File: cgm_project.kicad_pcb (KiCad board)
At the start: 2 copper layers, 50 x 70 mm, 34 parts, among them J1 JST BATT CONNECTOR, J2 USB_C_Receptacle_USB2.0_16P, J3 Conn_01x02, J4 Conn_01x02_MountingPin, Q1 AO3400, SW1 SW_SPDT, SW2 BOOT, SW3 RESET, U1 TP4056-42-ESOP8, U2 AP2112K-3.3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

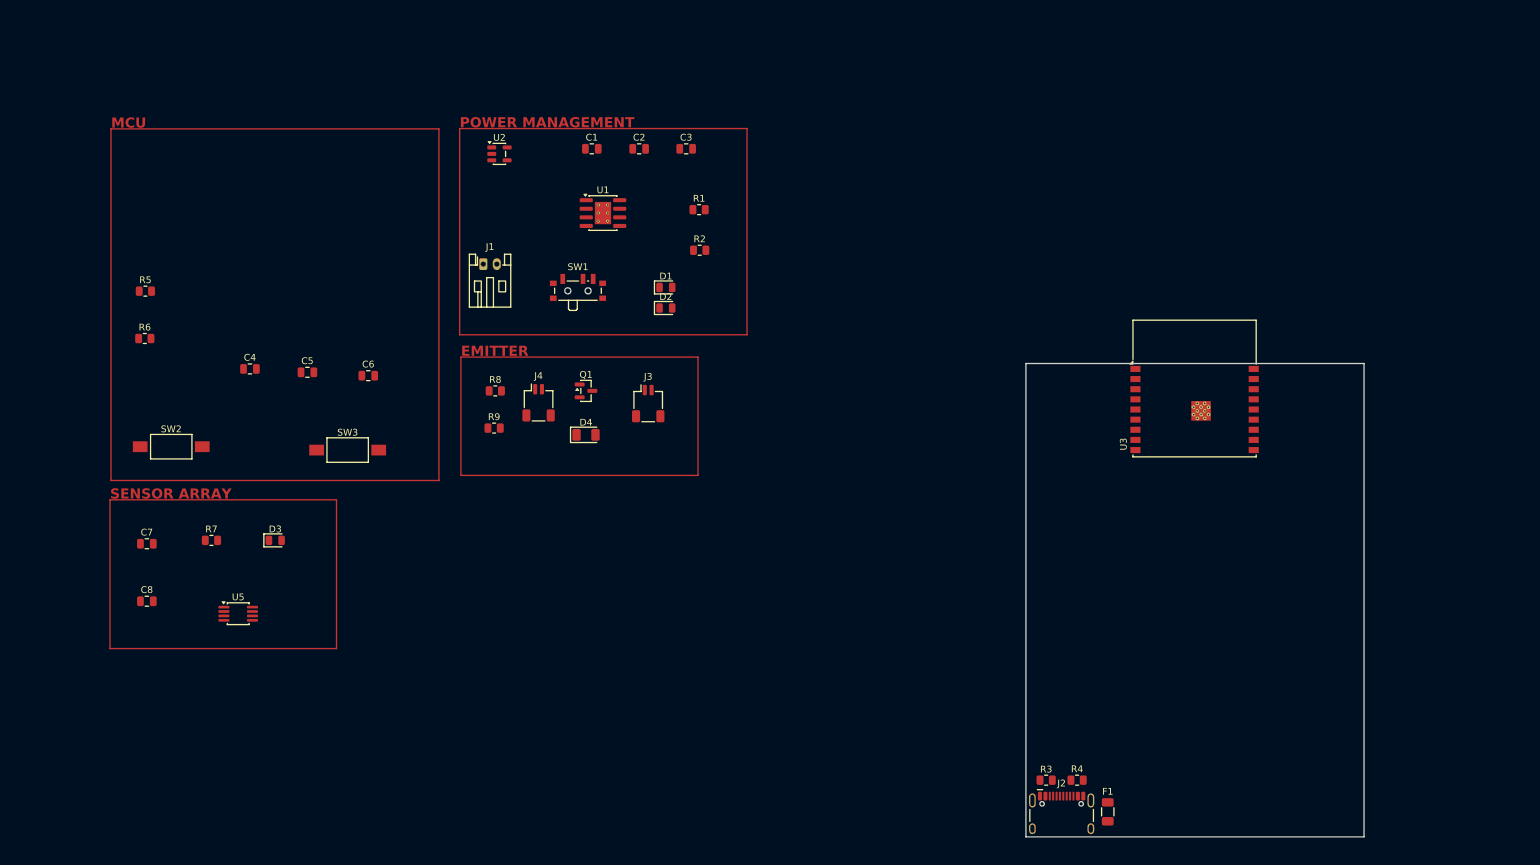
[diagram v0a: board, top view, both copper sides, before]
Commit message: chore: finalize component placement for power management, USB interface
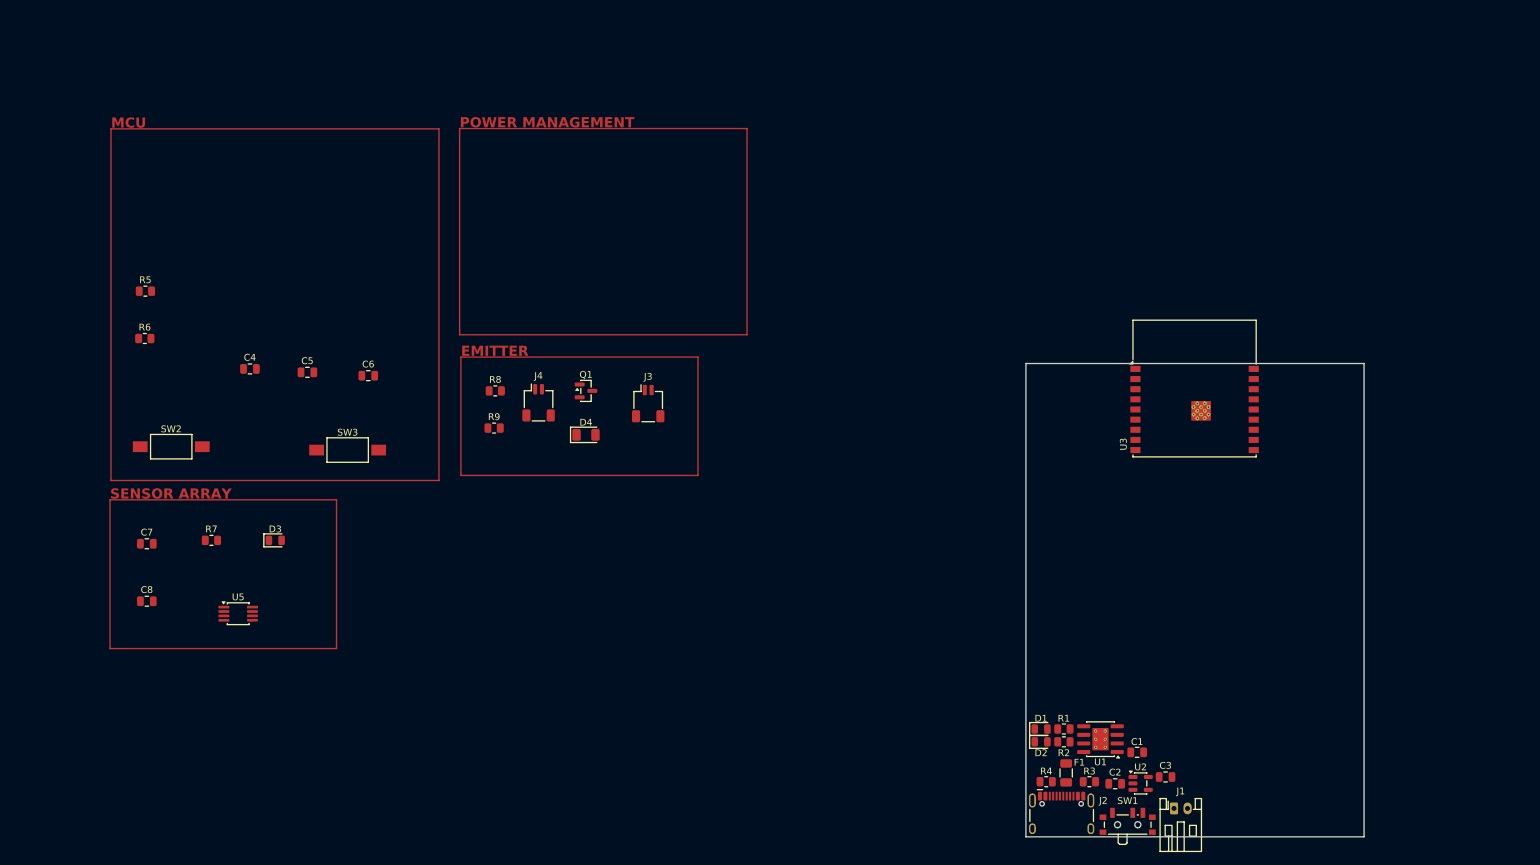
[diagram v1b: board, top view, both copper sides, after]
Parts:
- moved U2 132.9 mm to (167.0, 112.1)
- moved J1 130.1 mm to (171.9, 115.8)
- moved C1 120.3 mm to (166.4, 107.5), turned to 180 degrees
- moved C2 117.4 mm to (163.2, 112.2)
- moved C3 116.9 mm to (170.7, 111.2)
- moved SW1 113.3 mm to (165.1, 117.9)
- moved U1 107.1 mm to (161.0, 105.6), turned to 180 degrees
- moved R1 93.9 mm to (155.6, 104.0)
- moved R2 90.5 mm to (155.6, 106.0)
- moved D1 85.7 mm to (152.2, 104.1)
- moved D2 84.8 mm to (152.2, 106.0)
- moved F1 8.42 mm to (155.9, 110.5), turned to -90 degrees
- moved R3 6.40 mm to (159.4, 111.8)
- moved R4 4.57 mm to (153.0, 111.8), turned to 180 degrees

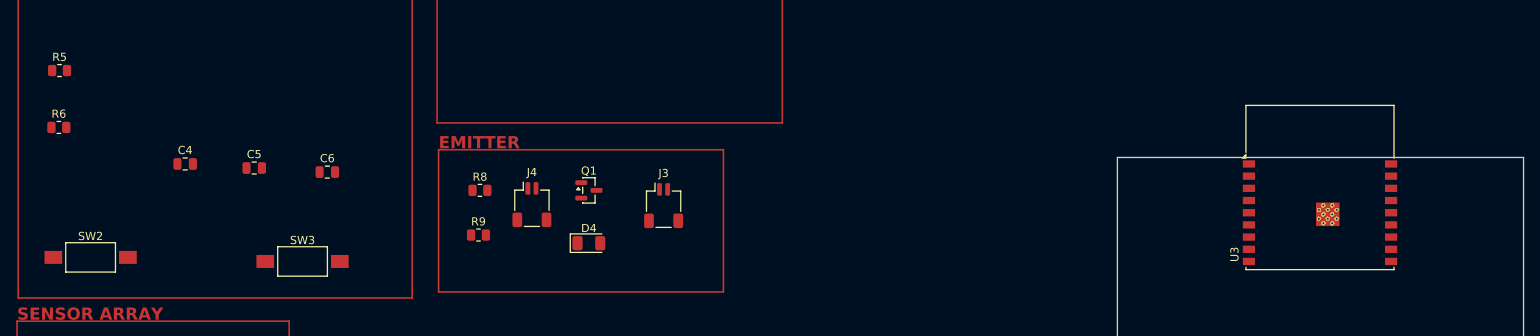
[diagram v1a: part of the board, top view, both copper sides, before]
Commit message: chore: finalize ESP32-C3 MCU layout, boot logic, and decoupling
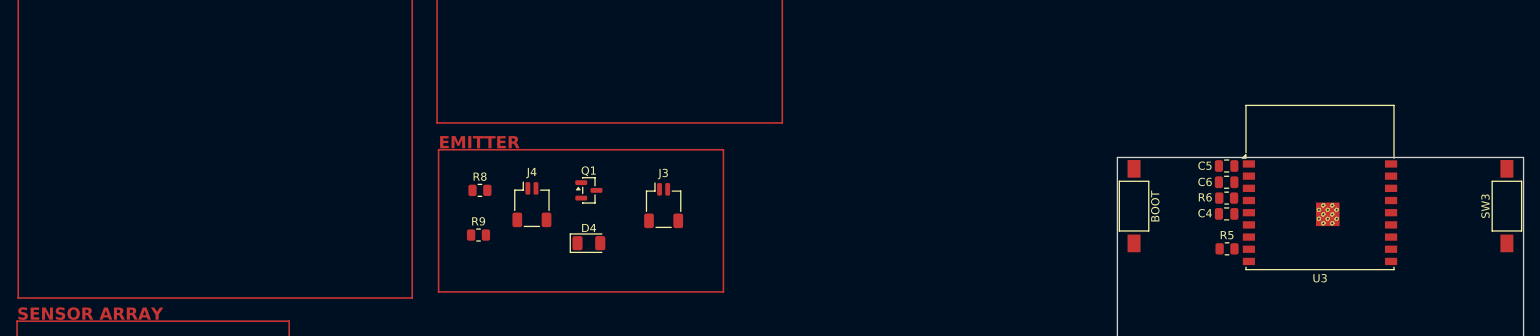
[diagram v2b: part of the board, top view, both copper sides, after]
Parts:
- moved SW3 148.4 mm to (197.9, 56.0), turned to 90 degrees
- moved R5 145.4 mm to (163.5, 61.2)
- moved R6 144.0 mm to (163.4, 55.0), turned to 180 degrees
- moved BOOT 128.6 mm to (152.1, 56.0), turned to 90 degrees
- moved C4 128.4 mm to (163.4, 57.0), turned to 180 degrees
- moved C5 119.7 mm to (163.4, 51.0), turned to 180 degrees
- moved C6 110.7 mm to (163.4, 53.0)
- renumbered SW2 to BOOT

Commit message: chore: finalize placement for analog sensor array
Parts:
- moved C7 161.9 mm to (177.3, 114.8), turned to -90 degrees
- moved C8 160.7 mm to (178.4, 112.1), turned to 180 degrees
- moved R7 157.3 mm to (182.7, 112.1)
- moved U5 150.6 mm to (181.5, 114.8), turned to 180 degrees
- moved D3 149.6 mm to (182.7, 117.5)
- moved C2 0.36 mm to (163.0, 111.8)
- renumbered SW3 to RESET
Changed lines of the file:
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@@
 	(footprint "Capacitor_SMD:C_0805_2012Metric"
 		(layer "F.Cu")
-		(at 19.995 76.655)
+		(at 177.35 114.8 -90)
 		(descr "Capacitor SMD 0805 (2012 Metric), square (rectangular) end terminal, IPC-7351 nominal, (Body size source: IPC-SM-782 page 76, https://www.pcb-3d.com/wordpress/wp-content/uploads/ipc-sm-782a_amendment_1_and_2.pdf, https://docs.google.com/spreadsheets/d/1BsfQQcO9C6DZCsRaXUlFlo91Tg2WpOkGARC1WS5S8t0/edit?usp=sharing)")
 		(tags "capacitor")
 		(property "Reference" "C7"
-			(at 0 -1.68 0)
+			(at 2.4 -0.05 180)
 			(layer "F.SilkS")
 			(effects
@@
 		)
 		(property "Value" "0.1uF"
-			(at -0.5 12.63 0)
+			(at -0.5 12.63 90)
 			(layer "F.Fab")
 			(effects
@@
 		)
 		(property "Datasheet" ""
-			(at 0 0 0)
+			(at 0 0 90)
 			(layer "F.Fab")
 			(hide yes)
@@
 		)
 		(property "Description" "Unpolarized capacitor, small symbol"
-			(at 0 0 0)
+			(at 0 0 90)
 			(layer "F.Fab")
 			(hide yes)
@@
 		)
 		(property "KiLib_Generator" "SMD_2terminal_chip_molded"
-			(at 0 0 0)
+			(at 0 0 90)
 			(layer "F.SilkS")
 			(hide yes)
@@
 		(duplicate_pad_numbers_are_jumpers no)
 		(fp_line
-			(start -0.261252 -0.735)
-			(end 0.261252 -0.735)
+			(start -0.261252 0.735)
+			(end 0.261252 0.735)
 			(stroke
 				(width 0.12)
@@
 		)
 		(fp_line
-			(start -0.261252 0.735)
-			(end 0.261252 0.735)
+			(start -0.261252 -0.735)
+			(end 0.261252 -0.735)
 			(stroke
 				(width 0.12)
@@
 		)
 		(fp_text user "${REFERENCE}"
-			(at 0 0 0)
+			(at 0 0 90)
 			(layer "F.Fab")
 			(effects
@@
 		)
 		(pad "1" smd roundrect
-			(at -0.95 0)
+			(at -0.95 0 270)
 			(size 1 1.45)
 			(layers "F.Cu" "F.Mask" "F.Paste")
@@
 		)
 		(pad "2" smd roundrect
-			(at 0.95 0)
+			(at 0.95 0 270)
 			(size 1 1.45)
 			(layers "F.Cu" "F.Mask" "F.Paste")
@@
 	(footprint "Capacitor_SMD:C_0805_2012Metric"
 		(layer "F.Cu")
-		(at 19.995 85.155)
+		(at 178.4 112.1 180)
 		(descr "Capacitor SMD 0805 (2012 Metric), square (rectangular) end terminal, IPC-7351 nominal, (Body size source: IPC-SM-782 page 76, https://www.pcb-3d.com/wordpress/wp-content/uploads/ipc-sm-782a_amendment_1_and_2.pdf, https://docs.google.com/spreadsheets/d/1BsfQQcO9C6DZCsRaXUlFlo91Tg2WpOkGARC1WS5S8t0/edit?usp=sharing)")
 		(tags "capacitor")
 		(property "Reference" "C8"
-			(at 0 -1.68 0)
+			(at 0 1.6 180)
 			(layer "F.SilkS")
 			(effects
@@
 		(duplicate_pad_numbers_are_jumpers no)
 		(fp_line
-			(start -0.261252 -0.735)
-			(end 0.261252 -0.735)
+			(start -0.261252 0.735)
+			(end 0.261252 0.735)
 			(stroke
 				(width 0.12)
@@
 		)
 		(fp_line
-			(start -0.261252 0.735)
-			(end 0.261252 0.735)
+			(start -0.261252 -0.735)
+			(end 0.261252 -0.735)
 			(stroke
 				(width 0.12)
@@
 		)
 		(pad "1" smd roundrect
-			(at -0.95 0)
+			(at -0.95 0 180)
 			(size 1 1.45)
 			(layers "F.Cu" "F.Mask" "F.Paste")
@@
 		)
 		(pad "2" smd roundrect
-			(at 0.95 0)
+			(at 0.95 0 180)
 			(size 1 1.45)
 			(layers "F.Cu" "F.Mask" "F.Paste")
@@
 	(footprint "Package_SO:MSOP-8_3x3mm_P0.65mm"
 		(layer "F.Cu")
-		(at 33.5 87)
+		(at 181.5125 114.825 180)
 		(descr "MSOP, 8 Pin (https://www.jedec.org/system/files/docs/mo-187F.pdf variant AA)")
 		(tags "MSOP SO")
 		(property "Reference" "U5"
-			(at 0 -2.45 0)
+			(at -4.0875 0.025 0)
 			(layer "F.SilkS")
 			(effects
@@
 		(duplicate_pad_numbers_are_jumpers no)
 		(fp_line
-			(start -1.61 -1.61)
-			(end 1.61 -1.61)
+			(start 1.61 1.61)
+			(end -1.61 1.61)
 			(stroke
 				(width 0.12)
@@
 		)
 		(fp_line
-			(start -1.61 -1.435)
-			(end -1.61 -1.61)
+			(start 1.61 1.435)
+			(end 1.61 1.61)
 			(stroke
 				(width 0.12)
@@
 		)
 		(fp_line
-			(start -1.61 1.61)
-			(end -1.61 1.435)
+			(start 1.61 -1.61)
+			(end 1.61 -1.435)
 			(stroke
 				(width 0.12)
@@
 		)
 		(fp_line
-			(start 1.61 -1.61)
-			(end 1.61 -1.435)
+			(start -1.61 1.61)
+			(end -1.61 1.435)
 			(stroke
 				(width 0.12)
@@
 		)
 		(fp_line
-			(start 1.61 1.435)
-			(end 1.61 1.61)
+			(start -1.61 -1.435)
+			(end -1.61 -1.61)
 			(stroke
 				(width 0.12)
@@
 		)
 		(fp_line
-			(start 1.61 1.61)
-			(end -1.61 1.61)
+			(start -1.61 -1.61)
+			(end 1.61 -1.61)
 			(stroke
 				(width 0.12)
@@
 		)
 		(fp_line
-			(start -3.18 -1.43)
-			(end -1.75 -1.43)
+			(start 3.18 1.43)
+			(end 1.75 1.43)
 			(stroke
 				(width 0.05)
@@
 		)
 		(fp_line
-			(start -3.18 1.43)
-			(end -3.18 -1.43)
+			(start 3.18 -1.43)
+			(end 3.18 1.43)
 			(stroke
 				(width 0.05)
@@
 		)
 		(fp_line
-			(start -1.75 -1.75)
-			(end 1.75 -1.75)
+			(start 1.75 1.75)
+			(end -1.75 1.75)
 			(stroke
 				(width 0.05)
@@
 		)
 		(fp_line
-			(start -1.75 -1.43)
-			(end -1.75 -1.75)
+			(start 1.75 1.43)
+			(end 1.75 1.75)
 			(stroke
 				(width 0.05)
@@
 		)
 		(fp_line
-			(start -1.75 1.43)
-			(end -3.18 1.43)
+			(start 1.75 -1.43)
+			(end 3.18 -1.43)
 			(stroke
 				(width 0.05)
@@
 		)
 		(fp_line
-			(start -1.75 1.75)
-			(end -1.75 1.43)
+			(start 1.75 -1.75)
+			(end 1.75 -1.43)
 			(stroke
 				(width 0.05)
@@
 		)
 		(fp_line
-			(start 1.75 -1.75)
-			(end 1.75 -1.43)
+			(start -1.75 1.75)
+			(end -1.75 1.43)
 			(stroke
 				(width 0.05)
@@
 		)
 		(fp_line
-			(start 1.75 -1.43)
-			(end 3.18 -1.43)
+			(start -1.75 1.43)
+			(end -3.18 1.43)
 			(stroke
 				(width 0.05)
@@
 		)
 		(fp_line
-			(start 1.75 1.43)
-			(end 1.75 1.75)
+			(start -1.75 -1.43)
+			(end -1.75 -1.75)
 			(stroke
 				(width 0.05)
@@
 		)
 		(fp_line
-			(start 1.75 1.75)
-			(end -1.75 1.75)
+			(start -1.75 -1.75)
+			(end 1.75 -1.75)
 			(stroke
 				(width 0.05)
@@
 		)
 		(fp_line
-			(start 3.18 -1.43)
-			(end 3.18 1.43)
+			(start -3.18 1.43)
+			(end -3.18 -1.43)
 			(stroke
 				(width 0.05)
@@
 		)
 		(fp_line
-			(start 3.18 1.43)
-			(end 1.75 1.43)
+			(start -3.18 -1.43)
+			(end -1.75 -1.43)
 			(stroke
 				(width 0.05)
@@
 		)
 		(pad "1" smd roundrect
-			(at -2.1125 -0.975)
+			(at -2.1125 -0.975 180)
 			(size 1.625 0.4)
 			(layers "F.Cu" "F.Mask" "F.Paste")
@@
 		)
 		(pad "2" smd roundrect
-			(at -2.1125 -0.325)
+			(at -2.1125 -0.325 180)
 			(size 1.625 0.4)
 			(layers "F.Cu" "F.Mask" "F.Paste")
@@
 		)
 		(pad "3" smd roundrect
-			(at -2.1125 0.325)
+			(at -2.1125 0.325 180)
 			(size 1.625 0.4)
 			(layers "F.Cu" "F.Mask" "F.Paste")
@@
 		)
 		(pad "4" smd roundrect
-			(at -2.1125 0.975)
+			(at -2.1125 0.975 180)
 			(size 1.625 0.4)
 			(layers "F.Cu" "F.Mask" "F.Paste")
@@
 		)
 		(pad "5" smd roundrect
-			(at 2.1125 0.975)
+			(at 2.1125 0.975 180)
 			(size 1.625 0.4)
 			(layers "F.Cu" "F.Mask" "F.Paste")
@@
 		)
 		(pad "6" smd roundrect
-			(at 2.1125 0.325)
+			(at 2.1125 0.325 180)
 			(size 1.625 0.4)
 			(layers "F.Cu" "F.Mask" "F.Paste")
@@
 		)
 		(pad "7" smd roundrect
-			(at 2.1125 -0.325)
+			(at 2.1125 -0.325 180)
 			(size 1.625 0.4)
 			(layers "F.Cu" "F.Mask" "F.Paste")
@@
 		)
 		(pad "8" smd roundrect
-			(at 2.1125 -0.975)
+			(at 2.1125 -0.975 180)
 			(size 1.625 0.4)
 			(layers "F.Cu" "F.Mask" "F.Paste")
@@
 	(footprint "LED_SMD:LED_0805_2012Metric"
 		(layer "F.Cu")
-		(at 38.9825 76.155)
+		(at 182.7125 117.55)
 		(descr "LED SMD 0805 (2012 Metric), square (rectangular) end terminal, IPC-7351 nominal, (Body size source: https://docs.google.com/spreadsheets/d/1BsfQQcO9C6DZCsRaXUlFlo91Tg2WpOkGARC1WS5S8t0/edit?usp=sharing)")
 		(tags "LED")
 		(property "Reference" "D3"
-			(at 0 -1.65 0)
+			(at 2.5625 -0.05 0)
 			(layer "F.SilkS")
 			(effects
@@
 		(descr "http://www.te.com/commerce/DocumentDelivery/DDEController?Action=srchrtrv&DocNm=1437566-3&DocType=Customer+Drawing&DocLang=English")
 		(tags "SPST button tactile switch")
-		(property "Reference" "SW3"
+		(property "Reference" "RESET"
 			(at 0 -2.6 90)
 			(layer "F.SilkS")
@@
 	(footprint "Capacitor_SMD:C_0805_2012Metric"
 		(layer "F.Cu")
-		(at 163.2 112.15)
+		(at 163 111.85)
 		(descr "Capacitor SMD 0805 (2012 Metric), square (rectangular) end terminal, IPC-7351 nominal, (Body size source: IPC-SM-782 page 76, https://www.pcb-3d.com/wordpress/wp-content/uploads/ipc-sm-782a_amendment_1_and_2.pdf, https://docs.google.com/spreadsheets/d/1BsfQQcO9C6DZCsRaXUlFlo91Tg2WpOkGARC1WS5S8t0/edit?usp=sharing)")
 		(tags "capacitor")
@@
 	(footprint "Resistor_SMD:R_0805_2012Metric"
 		(layer "F.Cu")
-		(at 29.545 76.155)
+		(at 182.7 112.1)
 		(descr "Resistor SMD 0805 (2012 Metric), square (rectangular) end terminal, IPC-7351 nominal, (Body size source: IPC-SM-782 page 72, https://www.pcb-3d.com/wordpress/wp-content/uploads/ipc-sm-782a_amendment_1_and_2.pdf)")
 		(tags "resistor")
 		(property "Reference" "R7"
-			(at 0 -1.65 0)
+			(at 0 -1.55 180)
 			(layer "F.SilkS")
 			(effects
